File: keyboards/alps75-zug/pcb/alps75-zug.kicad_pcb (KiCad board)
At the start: 2 copper layers, 176 parts, among them SW1 SW_Push, SW10 SW_Push, SW11 SW_Push, SW12 SW_Push, SW13 SW_Push, SW14 SW_Push, SW15 SW_Push, SW16 SW_Push, SW17 SW_Push, SW18 SW_Push, SW19 SW_Push, SW2 SW_Push, SW20 SW_Push, SW21 SW_Push, SW22 SW_Push, SW23 SW_Push, SW24 SW_Push, SW25 SW_Push, SW26 SW_Push, SW27 SW_Push, SW28 SW_Push, SW29 SW_Push, SW3 SW_Push, SW30 SW_Push, SW31 SW_Push, SW32 SW_Push, SW33 SW_Push, SW34 SW_Push, SW35 SW_Push, SW36 SW_Push, SW37 SW_Push, SW38 SW_Push, SW39 SW_Push, SW4 SW_Push, SW40 SW_Push, SW41 SW_Push, SW42 SW_Push, SW43 SW_Push, SW44 SW_Push, SW45 SW_Push, SW46 SW_Push, SW47 SW_Push, SW48 SW_Push, SW49 SW_Push, SW5 SW_Push, SW50 SW_Push, SW51 SW_Push, SW52 SW_Push, SW53 SW_Push, SW54 SW_Push, SW55 SW_Push, SW56 SW_Push, SW57 SW_Push, SW58 SW_Push, SW59 SW_Push, SW6 SW_Push, SW60 SW_Push, SW61 SW_Push, SW62 SW_Push, SW63 SW_Push, SW64 SW_Push, SW65 SW_Push, SW66 SW_Push, SW67 SW_Push, SW68 SW_Push, SW69 SW_Push, SW7 SW_Push, SW70 SW_Push, SW71 SW_Push, SW72 SW_Push, SW73 SW_Push, SW74 SW_Push, SW75 SW_Push, SW76 SW_Push, SW77 SW_Push, SW78 SW_Push, SW79 SW_Push, SW8 SW_Push, SW80 SW_Push, SW81 SW_Push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

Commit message: Derive the alps75-zug board outline, mounting holes and stab slots from the plate
The board had no Edge.Cuts geometry and no mounting holes at all. All of
this now comes from alps75-zug-keyboard-plate.jscad, with y negated since
the plate is authored y-up and KiCad is y-down:

- Edge.Cuts is the plate outline: 340.3 x 130.735 mm, 4 mm corner radius,
  x -17.75..322.55, y -16.4005..114.3345.
- H1..H8 are MountingHole_3.2mm_M3 at the plate's eight drill positions
  (y 12.4 top / -110.335 bottom in plate coords). The exported Excellon
  matches the plate hole set exactly, tool T2C3.200, no extras, none
  missing.
- The twelve Alps AEK stabiliser slots are reproduced on Dwgs.User as
  documentation outlines only. AEK stabs are plate-mount -- the insert
  clips into the plate and the wire runs in the plate-to-PCB gap -- and
  ai03's Alps_Solderable footprints put no stab holes on the PCB either,
  so cutting them here would only cost routing area.

H1..H8 are in the schematic too, so the next "Update PCB from Schematic"
does not delete the footprints.

DRC 0 violations, ERC 0 violations, schematic parity clean for everything
added (the 88 remaining parity warnings are the pre-existing Sim.Device
field mismatch on the kbplacer-generated diodes).

Co-Authored-By: Claude Opus 5 <noreply@anthropic.com>
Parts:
- added H1: MountingHole_3.2mm_M3, MountingHole:MountingHole_3.2mm_M3, F.Cu at (-13.8, -12.4)
- added H2: MountingHole_3.2mm_M3, MountingHole:MountingHole_3.2mm_M3, F.Cu at (66.7, -12.4)
- added H3: MountingHole_3.2mm_M3, MountingHole:MountingHole_3.2mm_M3, F.Cu at (219.1, -12.4)
- added H4: MountingHole_3.2mm_M3, MountingHole:MountingHole_3.2mm_M3, F.Cu at (318.6, -12.4)
- added H5: MountingHole_3.2mm_M3, MountingHole:MountingHole_3.2mm_M3, F.Cu at (-13.8, 110.3)
- added H6: MountingHole_3.2mm_M3, MountingHole:MountingHole_3.2mm_M3, F.Cu at (66.7, 110.3)
- added H7: MountingHole_3.2mm_M3, MountingHole:MountingHole_3.2mm_M3, F.Cu at (219.1, 110.3)
- added H8: MountingHole_3.2mm_M3, MountingHole:MountingHole_3.2mm_M3, F.Cu at (318.6, 110.3)
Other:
- board outline added: 340.3 x 130.7 mm
- board text added: "Alps AEK stabiliser slots (plate-mount) - plate cutout outlines, no PCB cutout; keep tall parts clear"
- board text added: "Board outline = keyboard plate outline 340.3 x 130.735 mm, corner radius 4 mm"

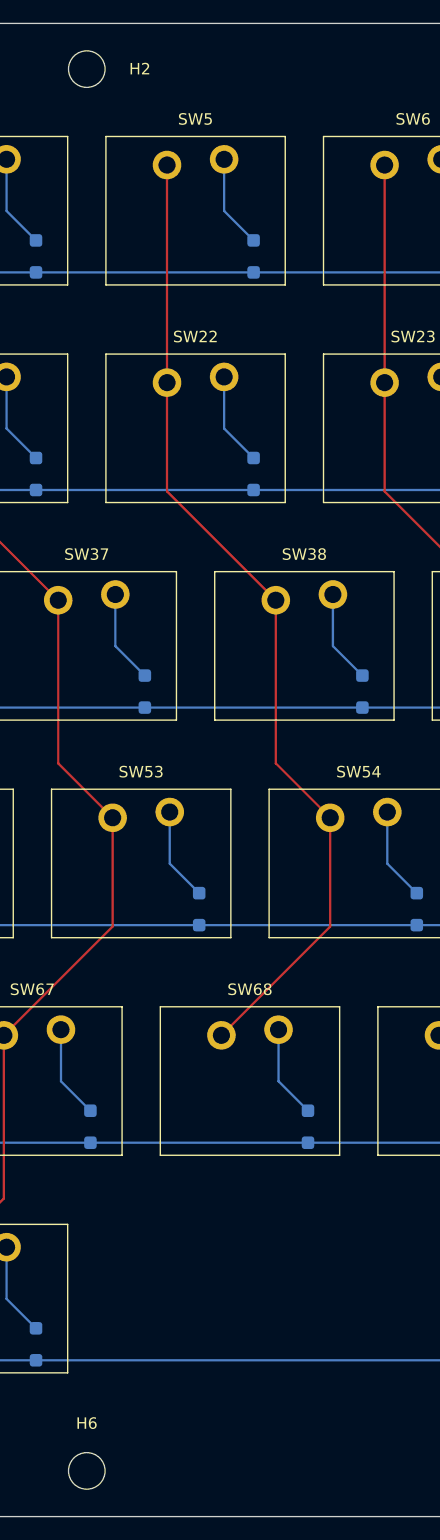
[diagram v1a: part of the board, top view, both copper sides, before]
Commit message: Make the alps75-zug custom mounting holes symmetric about the board centre
The custom holes were at x 66.675 and 219.075, which are 85.725 and
66.675 from the board centre at 152.4 -- not a mirror pair. The
asymmetry was unintentional. Moving the left pair to 85.725 mirrors
219.075 exactly and keeps both on the key-column grid (85.725 is the
"2,4" column, 219.075 the "2,11").

Edge spans go from 80.425 / 152.4 / 99.475 to 99.475 / 133.35 / 99.475
on both the front and back edges, so the longest unsupported run drops
by 19 mm as well. The back edge keeps 126.5 mm of clear strip centred on
x 152.4 for USB-C, and the 62.5 x 31.2 mm pocket under the right half of
the spacebar -- the intended spot for the RP2040 subsystem -- is
untouched.

Exported Excellon still matches the plate's eight holes exactly. DRC 0
violations, ERC 0 violations.

Co-Authored-By: Claude Opus 5 <noreply@anthropic.com>
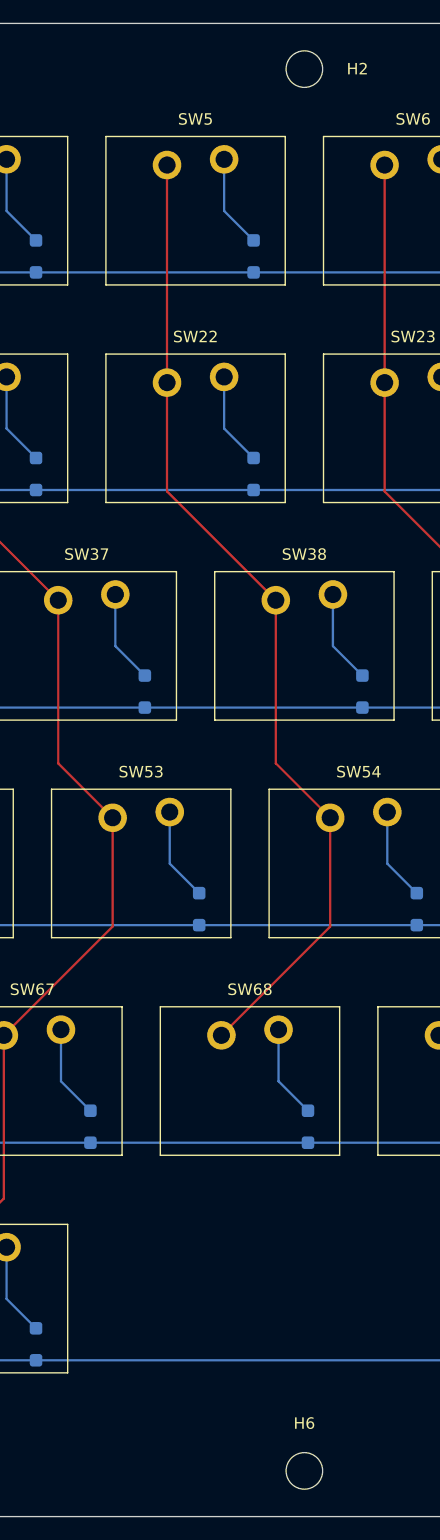
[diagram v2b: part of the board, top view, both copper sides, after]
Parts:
- moved H2 19.0 mm to (85.7, -12.4)
- moved H6 19.0 mm to (85.7, 110.3)
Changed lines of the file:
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@@
 	(footprint "MountingHole:MountingHole_3.2mm_M3"
 		(layer "F.Cu")
-		(at 66.675 -12.4)
+		(at 85.725 -12.4)
 		(descr "Mounting Hole 3.2mm, M3, no annular, generated by kicad-footprint-generator mountinghole.py")
 		(tags "mountinghole M3")
@@
 	(footprint "MountingHole:MountingHole_3.2mm_M3"
 		(layer "F.Cu")
-		(at 66.675 110.335)
-		(descr "Mounting Hole 3.2mm, M3, no annular, generated by kicad-footprint-generator mountinghole.py")
-		(tags "mountinghole M3")
+		(at 85.725 110.335)
+		(descr "Mounting Hole 3.2mm, M3, no annular, generated by kicad-footprint-generator mountinghole.py")
+		(tags "mountinghole M3")

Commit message: Move to A2 sheet to contain design
Also drops the two Dwgs.User annotation notes that were removed in the
same KiCad session.

Co-Authored-By: Claude Opus 5 <noreply@anthropic.com>
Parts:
- moved D15 161.2 mm to (410.9, 85.3)
- moved D16 161.2 mm to (430.0, 85.3)
- moved D32 161.2 mm to (430.0, 104.3)
- moved D47 161.2 mm to (406.2, 123.4)
- moved D48 161.2 mm to (430.0, 123.4)
- moved D62 161.2 mm to (399.0, 142.4)
- moved D63 161.2 mm to (430.0, 142.4)
- moved D70 161.2 mm to (263.3, 161.5)
- moved D77 161.2 mm to (430.0, 161.5)
- moved D86 161.2 mm to (410.9, 180.6)
- moved D87 161.2 mm to (430.0, 180.6)
- moved H3 161.2 mm to (358.2, 68.9)
- moved H7 161.2 mm to (358.2, 191.6)
- moved SW10 161.2 mm to (310.6, 81.3)
- moved SW15 161.2 mm to (405.8, 81.3)
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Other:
- board text removed: "Alps AEK stabiliser slots (plate-mount) - plate cutout outlines, no PCB cutout; keep tall parts clear"
- board text removed: "Board outline = keyboard plate outline 340.3 x 130.735 mm, corner radius 4 mm"

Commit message: Add key legends to the alps75-zug front silkscreen
One F.SilkS text per switch, derived from the layout.json key labels and
anchored on each switch footprint's own origin, 3.5 mm below centre where
the footprint interior is clear of the two Alps pads.

Dual-legend keys carry the unshifted/base character (1, not !; ` not ~;
[ not {), and the two 1.25u modifiers read "option". The two bottom-row
keys still marked "." in layout.json are undecided and carry "??".

Co-Authored-By: Claude Opus 5 <noreply@anthropic.com>
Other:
- board text added: "'"
- board text added: ","
- board text added: "-"
- board text added: "."
- board text added: "/"
- board text added: "0"
- board text added: "1"
- board text added: "2"
- board text added: "3"
- board text added: "4"
- board text added: "5"
- board text added: "6"
- board text added: "7"
- board text added: "8"
- board text added: "9"
- board text added: ";"
- board text added: "="
- board text added: "??"
- board text added: "A"
- board text added: "B"
- board text added: "C"
- board text added: "D"
- board text added: "E"
- board text added: "F"
- board text added: "F1"
- board text added: "F10"
- board text added: "F11"
- board text added: "F12"
- board text added: "F13"
- board text added: "F14"
- board text added: "F15"
- board text added: "F2"
- board text added: "F3"
- board text added: "F4"
- board text added: "F5"
- board text added: "F6"
- board text added: "F7"
- board text added: "F8"
- board text added: "F9"
- board text added: "G"
- board text added: "H"
- board text added: "I"
- board text added: "J"
- board text added: "K"
- board text added: "L"
- board text added: "M"
- board text added: "N"
- board text added: "O"
- board text added: "P"
- board text added: "Q"
- board text added: "R"
- board text added: "S"
- board text added: "T"
- board text added: "U"
- board text added: "V"
- board text added: "W"
- board text added: "X"
- board text added: "Y"
- board text added: "Z"
- board text added: "["
- board text added: "\"
- board text added: "]"
- board text added: "`"
- board text added: "caps lock"
- board text added: "command"
- board text added: "control"
- board text added: "del"
- board text added: "delete"
- board text added: "end"
- board text added: "esc"
- board text added: "home"
- board text added: "option"
- board text added: "pgdn"
- board text added: "pgup"
- board text added: "play/pause"
- board text added: "return"
- board text added: "shift"
- board text added: "space"
- board text added: "tab"
- board text added: "vol+"
- board text added: "vol-"
- board text added: "←"
- board text added: "↑"
- board text added: "→"
- board text added: "↓"
